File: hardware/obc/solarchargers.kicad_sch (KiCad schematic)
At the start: 36 parts, among them U105 LTC4121, U106 LTC4121

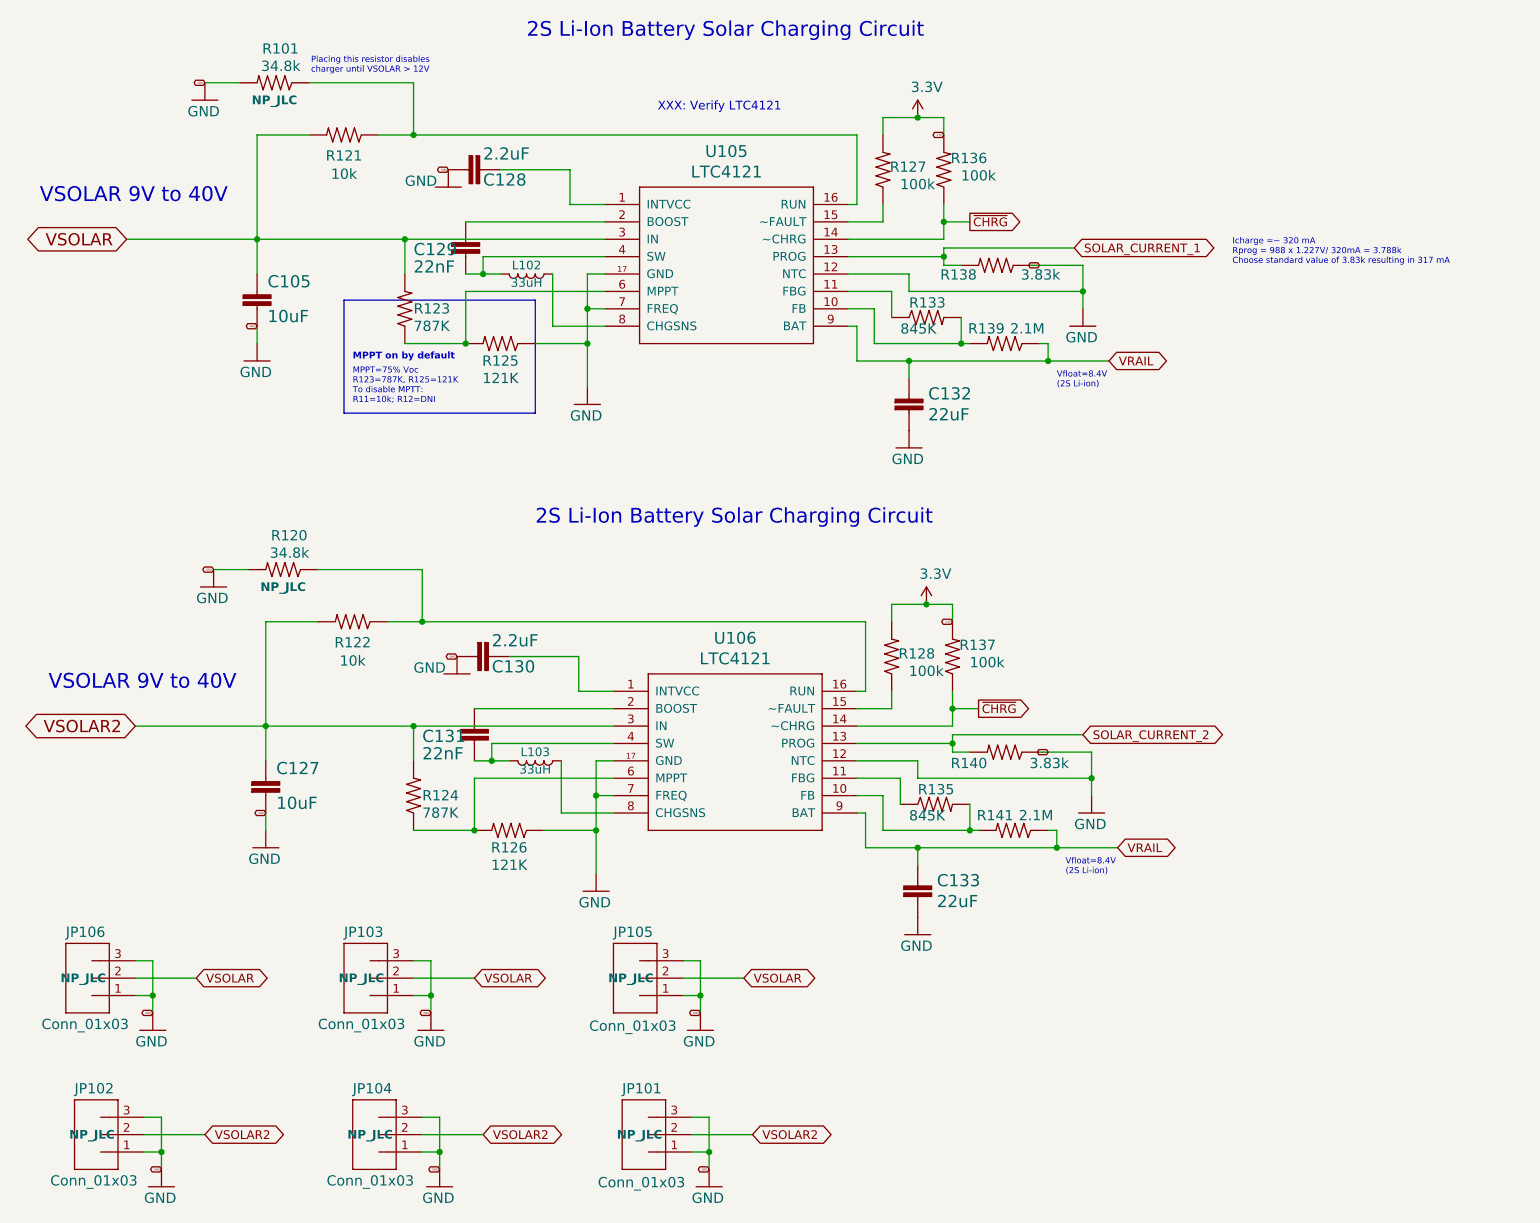
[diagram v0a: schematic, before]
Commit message: obc: BOM and schematic cleanup
- remove unused fields
- remove incorrect datasheets
- fix a connector 'value' field (CONx02 instead of x05)
- add documentation to power supervisor page

This is in preparation for a comprehensive review pass by me.

In the layout, some issues were identified (QSPI_* pins routed
suboptimally, silkscreen on pads, and some layer reduction could
take place.  Bouncing this back to Luke for further work before
my review pass there.
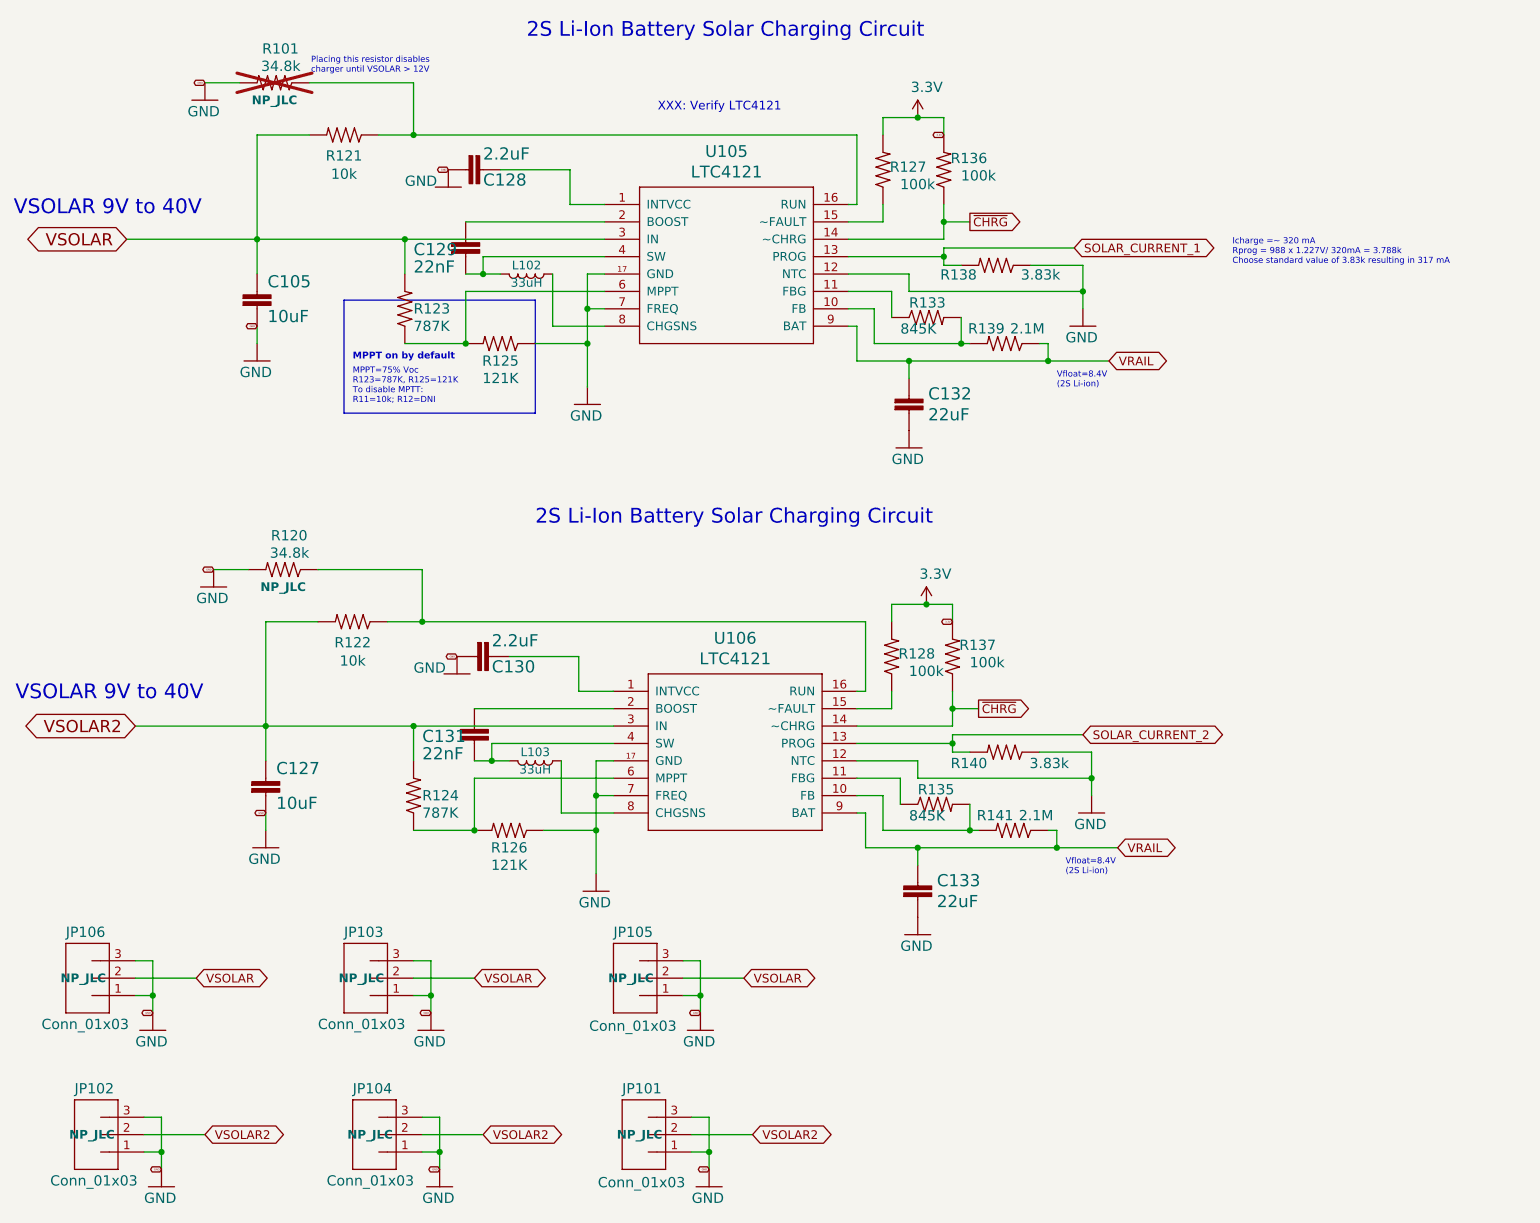
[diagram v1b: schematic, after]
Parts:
- JP101, JP102, JP103, JP104, JP105, JP106: Flight 22-23-2037 -> (none); Proto 22-23-2037 -> (none)
- L102, L103: Flight SLF6028T-330MR69-PF -> (none); Proto SNR5040K-330M -> (none)
- R101: now not fitted
- U105, U106: Flight LTC4121EUD -> (none); Proto LTC4121EUD -> (none)

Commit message: obc: cleaned up BOM and re-routed MRAM and PSRAM
- cleaned up notes that no longer applied and changed some LCSC part numbers
- Gave QSPI_CLK a better route
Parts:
- C105, C127: LCSC C85713 -> C344022; Manufacturer_Name Samsung Electro-Mechanics -> (none); Manufacturer_Part_Number CL10A106MP8NNNC -> (none); Notes 10V ok? -> (none)
- C132, C133: LCSC C84419 -> C2762594; Manufacturer_Name Murata Electronics -> (none); Manufacturer_Part_Number GRM188R61A226ME15D -> (none); Notes 10V ok? -> (none)
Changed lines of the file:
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@@
 			)
 		)
-		(property "Description" "10V 10uF X5R ±20% 0603"
+		(property "Description" ""
 			(at 50.8 130.81 0)
 			(effects
@@
 			)
 		)
-		(property "LCSC" "C85713"
+		(property "LCSC" "C344022"
 			(at 50.8 130.81 0)
 			(effects
@@
 			)
 		)
-		(property "Manufacturer_Name" " Samsung Electro-Mechanics"
+		(property "Manufacturer_Name" ""
 			(at 50.8 130.81 0)
 			(effects
@@
 			)
 		)
-		(property "Manufacturer_Part_Number" "CL10A106MP8NNNC"
+		(property "Manufacturer_Part_Number" ""
 			(at 50.8 130.81 0)
 			(effects
@@
 			)
 		)
-		(property "Notes" "10V ok?"
+		(property "Notes" ""
 			(at 50.8 130.81 0)
 			(effects
@@
 			)
 		)
-		(property "Description" "10V 10uF X5R ±20% 0603"
+		(property "Description" ""
 			(at 49.53 59.69 0)
 			(effects
@@
 			)
 		)
-		(property "LCSC" "C85713"
+		(property "LCSC" "C344022"
 			(at 49.53 59.69 0)
 			(effects
@@
 			)
 		)
-		(property "Manufacturer_Name" " Samsung Electro-Mechanics"
+		(property "Manufacturer_Name" ""
 			(at 49.53 59.69 0)
 			(effects
@@
 			)
 		)
-		(property "Manufacturer_Part_Number" "CL10A106MP8NNNC"
+		(property "Manufacturer_Part_Number" ""
 			(at 49.53 59.69 0)
 			(effects
@@
 			)
 		)
-		(property "Notes" "10V ok?"
+		(property "Notes" ""
 			(at 49.53 59.69 0)
 			(effects
@@
 			)
 		)
-		(property "Description" "10V 22uF X5R ±20% 0603"
+		(property "Description" ""
 			(at 144.78 74.93 0)
 			(effects
@@
 			)
 		)
-		(property "LCSC" "C84419"
+		(property "LCSC" "C2762594"
 			(at 144.78 74.93 0)
 			(effects
@@
 			)
 		)
-		(property "Manufacturer_Name" " Murata Electronics"
+		(property "Manufacturer_Name" ""
 			(at 144.78 74.93 0)
 			(effects
@@
 			)
 		)
-		(property "Manufacturer_Part_Number" " GRM188R61A226ME15D"
+		(property "Manufacturer_Part_Number" ""
 			(at 144.78 74.93 0)
 			(effects
@@
 			)
 		)
-		(property "Notes" "10V ok?"
+		(property "Notes" ""
 			(at 144.78 74.93 0)
 			(effects
@@
 			)
 		)
-		(property "Description" "10V 22uF X5R ±20% 0603"
+		(property "Description" ""
 			(at 146.05 146.05 0)
 			(effects
@@
 			)
 		)
-		(property "LCSC" "C84419"
+		(property "LCSC" "C2762594"
 			(at 146.05 146.05 0)
 			(effects
@@
 			)
 		)
-		(property "Manufacturer_Name" " Murata Electronics"
+		(property "Manufacturer_Name" ""
 			(at 146.05 146.05 0)
 			(effects
@@
 			)
 		)
-		(property "Manufacturer_Part_Number" " GRM188R61A226ME15D"
+		(property "Manufacturer_Part_Number" ""
 			(at 146.05 146.05 0)
 			(effects
@@
 			)
 		)
-		(property "Notes" "10V ok?"
+		(property "Notes" ""
 			(at 146.05 146.05 0)
 			(effects

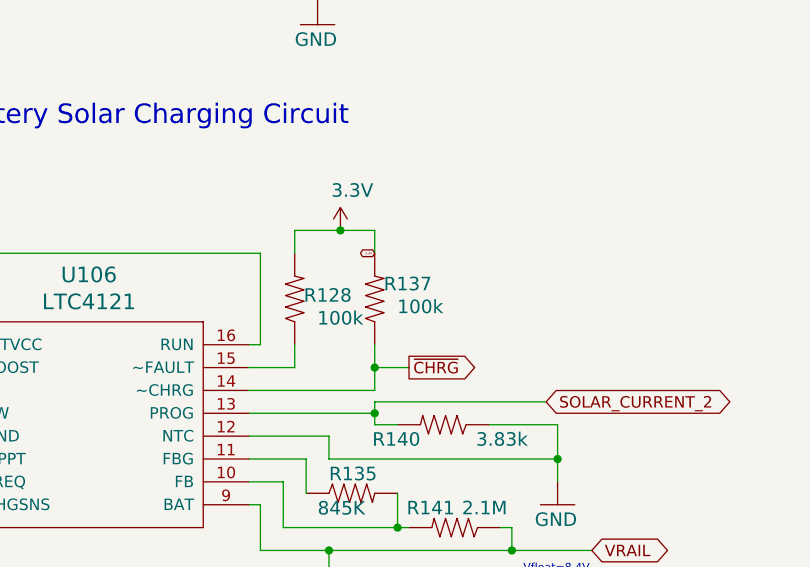
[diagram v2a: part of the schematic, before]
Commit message: ob: revised BOM and cleaned up PCB traces
- fixed BOM issues noticed
- added 2 extra capacitors on vwatchedrail and near 3.3v regulator
- cleaned up traces and did layer reduction
- moved whole watchdog circuit to a better location so all components can be close together
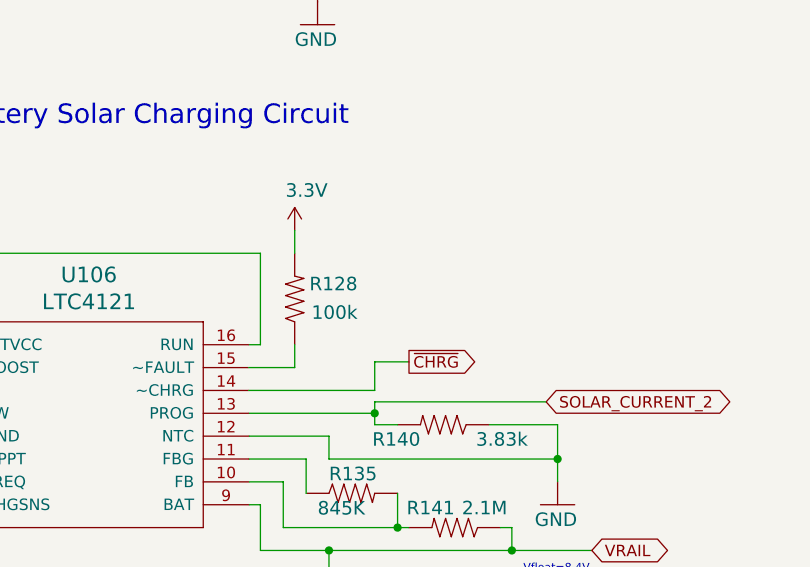
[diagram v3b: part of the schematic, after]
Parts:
- removed R137: 100k, Resistor_SMD:R_0603_1608Metric, symbol mainboard:R-US_R0603
- R121, R122: LCSC C169849 -> C191124
- R133, R135: LCSC C246013 -> C2091473
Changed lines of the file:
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@@
 	)
 	(junction
-		(at 151.13 118.11)
-		(diameter 0)
-		(color 0 0 0 0)
-	)
-	(junction
 		(at 76.2 182.88)
 		(diameter 0)
@@
 	)
 	(junction
-		(at 147.32 102.87)
-		(diameter 0)
-		(color 0 0 0 0)
-	)
-	(junction
 		(at 72.39 120.65)
 		(diameter 0)
@@
 	(wire
 		(pts
-			(xy 151.13 118.11) (xy 154.94 118.11)
+			(xy 151.13 117.475) (xy 154.94 117.475)
 		)
 		(stroke
@@
 	(wire
 		(pts
-			(xy 147.32 102.87) (xy 151.13 102.87)
-		)
-		(stroke
-			(width 0)
-			(type default)
-		)
-	)
-	(wire
-		(pts
 			(xy 165.1 67.31) (xy 173.99 67.31)
 		)
@@
 	(wire
 		(pts
-			(xy 151.13 115.57) (xy 151.13 118.11)
-		)
-		(stroke
-			(width 0)
-			(type default)
-		)
-	)
-	(wire
-		(pts
 			(xy 50.8 133.35) (xy 50.8 135.89)
 		)
@@
 	(wire
 		(pts
-			(xy 142.24 102.87) (xy 147.32 102.87)
-		)
-		(stroke
-			(width 0)
-			(type default)
-		)
-	)
-	(wire
-		(pts
 			(xy 101.6 120.65) (xy 72.39 120.65)
 		)
@@
 	(wire
 		(pts
-			(xy 151.13 118.11) (xy 151.13 120.65)
+			(xy 151.13 117.475) (xy 151.13 120.65)
 		)
 		(stroke
@@
 	(wire
 		(pts
-			(xy 151.13 105.41) (xy 151.13 102.87)
-		)
-		(stroke
-			(width 0)
-			(type default)
-		)
-	)
-	(wire
-		(pts
 			(xy 57.15 34.29) (xy 49.53 34.29)
 		)
@@
 		)
 	)
-	(global_label "3.3V"
-		(shape bidirectional)
-		(at 151.13 105.41 180)
-		(effects
-			(font
-				(size 0.254 0.254)
-			)
-			(justify right)
-		)
-		(property "Intersheetrefs" "${INTERSHEET_REFS}"
-			(at 151.13 105.41 0)
-			(effects
-				(font
-					(size 1.27 1.27)
-				)
-				(hide yes)
-			)
-		)
-	)
 	(global_label "VSOLAR2"
 		(shape bidirectional)
@@
 	(global_label "~{CHRG}"
 		(shape output)
-		(at 154.94 118.11 0)
+		(at 154.94 117.475 0)
 		(effects
 			(font
@@
 		)
 		(property "Intersheetrefs" "${INTERSHEET_REFS}"
-			(at 154.94 118.11 0)
+			(at 154.94 117.475 0)
 			(effects
 				(font
@@
 	)
 	(symbol
-		(lib_id "mainboard:R-US_R0603")
-		(at 151.13 110.49 90)
-		(unit 1)
-		(exclude_from_sim no)
-		(in_bom yes)
-		(on_board yes)
-		(dnp no)
-		(property "Reference" "R137"
-			(at 157.48 107.95 90)
-			(effects
-				(font
-					(size 1.4986 1.4986)
-				)
-				(justify left bottom)
-			)
-		)
-		(property "Value" "100k"
-			(at 158.75 110.49 90)
-			(effects
-				(font
-					(size 1.4986 1.4986)
-				)
-				(justify left bottom)
-			)
-		)
-		(property "Footprint" "Resistor_SMD:R_0603_1608Metric"
-			(at 151.13 110.49 0)
-			(effects
-				(font
-					(size 1.27 1.27)
-				)
-				(hide yes)
-			)
-		)
-		(property "Datasheet" ""
-			(at 151.13 110.49 0)
-			(effects
-				(font
-					(size 1.27 1.27)
-				)
-				(hide yes)
-			)
-		)
-		(property "Description" "100K 0603"
-			(at 154.94 107.95 0)
-			(effects
-				(font
-					(size 1.27 1.27)
-				)
-				(hide yes)
-			)
-		)
-		(property "LCSC" "C5369222"
-			(at 151.13 110.49 0)
-			(effects
-				(font
-					(size 1.27 1.27)
-				)
-				(hide yes)
-			)
-		)
-		(property "Manufacturer_Name" "Vishay Intertech"
-			(at 151.13 110.49 0)
-			(effects
-				(font
-					(size 1.27 1.27)
-				)
-				(hide yes)
-			)
-		)
-		(property "Manufacturer_Part_Number" "CRCW0603100KFKEC"
-			(at 151.13 110.49 0)
-			(effects
-				(font
-					(size 1.27 1.27)
-				)
-				(hide yes)
-			)
-		)
-		(property "Notes" ""
-			(at 151.13 110.49 0)
-			(effects
-				(font
-					(size 1.27 1.27)
-				)
-				(hide yes)
-			)
-		)
-		(property "Height" ""
-			(at 151.13 110.49 0)
-			(effects
-				(font
-					(size 1.27 1.27)
-				)
-				(hide yes)
-			)
-		)
-		(property "Sim.Type" ""
-			(at 151.13 110.49 0)
-			(effects
-				(font
-					(size 1.27 1.27)
-				)
-				(hide yes)
-			)
-		)
-		(pin "2"
-		)
-		(pin "1"
-		)
-		(instances
-			(project "mainboard"
-				(path "/e3ac22ea-6806-4807-a025-571315789c25/5728bec1-e38c-4cf8-8d7a-17e9d882a72f"
-					(reference "R137")
-					(unit 1)
-				)
-			)
-		)
-	)
-	(symbol
 		(lib_id "mainboard:2.2UF-0603-10V-20%")
 		(at 81.28 110.49 270)
@@
 			)
 		)
-		(property "LCSC" "C246013"
+		(property "LCSC" "C2091473"
 			(at 148.59 132.08 0)
 			(effects
@@
 			)
 		)
-		(property "LCSC" "C246013"
+		(property "LCSC" "C2091473"
 			(at 147.32 60.96 0)
 			(effects
@@
 			)
 		)
-		(property "LCSC" "C169849"
+		(property "LCSC" "C191124"
 			(at 62.23 34.29 0)
 			(effects
@@
 			)
 		)
-		(property "LCSC" "C169849"
+		(property "LCSC" "C191124"
 			(at 63.5 105.41 0)
 			(effects
@@
 		(dnp no)
 		(property "Reference" "R128"
-			(at 148.59 109.22 90)
+			(at 149.225 107.95 90)
 			(effects
 				(font
@@
 		)
 		(property "Value" "100k"
-			(at 149.86 111.76 90)
+			(at 149.225 111.125 90)
 			(effects
 				(font
@@
 	(symbol
 		(lib_id "mainboard:3.3V")
-		(at 147.32 102.87 0)
+		(at 142.24 102.87 0)
 		(unit 1)
 		(exclude_from_sim no)
@@
 		(dnp no)
 		(property "Reference" "#P+0102"
-			(at 147.32 102.87 0)
+			(at 142.24 102.87 0)
 			(effects
 				(font
@@
 		)
 		(property "Value" "3.3V"
-			(at 146.304 99.314 0)
+			(at 141.224 99.314 0)
 			(effects
 				(font
@@
 		)
 		(property "Footprint" ""
-			(at 147.32 102.87 0)
+			(at 142.24 102.87 0)
 			(effects
 				(font
@@
 		)
 		(property "Datasheet" ""
-			(at 147.32 102.87 0)
+			(at 142.24 102.87 0)
 			(effects
 				(font
@@
 		)
 		(property "Description" ""
-			(at 147.32 102.87 0)
+			(at 142.24 102.87 0)
 			(effects
 				(font
